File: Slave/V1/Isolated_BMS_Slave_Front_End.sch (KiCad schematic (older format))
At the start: 23 parts, among them J102 1935161, Q101 CPH6347-TL-W, U101 SI8641AB-B-IS1

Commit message: clear annotation
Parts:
- removed R103: RC0805JR-071KL, Resistors:R0805, symbol RC0805JR-071KL
- added R?: RC0805JR-07470KL, Resistors:R0805, symbol RC0805JR-07470KL
- renumbered C102 to C?, C101 to C?, C103 to C?, J102 to J?, Q101 to Q?, R101 to R?, U101 to U?
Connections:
- wire segments 115 -> 95
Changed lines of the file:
@@
 $EndDescr
 $Comp
-L CPH6347-TL-W Q101
+L CPH6347-TL-W Q?
 U 1 1 591B47DF
 P 2100 1300
-F 0 "Q101" V 2500 1300 60  0000 C CNN
+F 0 "Q?" V 2500 1300 60  0000 C CNN
 F 1 "CPH6347-TL-W" V 2400 1200 60  0000 C CNN
 F 2 "IC:TSOT-23-6" H 2200 400 60  0001 C CNN
@@
 $EndComp
 $Comp
-L 1935161 J102
+L 1935161 J?
 U 1 1 591B7F13
 P 900 1300
-F 0 "J102" H 800 1500 60  0000 C CNN
+F 0 "J?" H 800 1500 60  0000 C CNN
 F 1 "1935161" H 900 980 50  0001 C CNN
 F 2 "Connectors:1935161" H 900 390 30  0001 C CNN
@@
 CELL_Voltage
 $Comp
-L SI8641AB-B-IS1 U101
+L SI8641AB-B-IS1 U?
 U 1 1 591D60B1
 P 6200 4600
-F 0 "U101" H 6200 5400 60  0000 C CNN
+F 0 "U?" H 6200 5400 60  0000 C CNN
 F 1 "SI8641AB-B-IS1" H 6200 3750 60  0000 C CNN
 F 2 "IC:SOIC-16" H 6200 2800 60  0001 C CNN
@@
 $EndComp
 $Comp
-L AGND #PWR04
+L AGND #PWR?
 U 1 1 591D612D
 P 7600 4000
-F 0 "#PWR04" H 7600 3830 50  0001 C CNN
+F 0 "#PWR?" H 7600 3830 50  0001 C CNN
 F 1 "AGND" H 7600 3900 50  0000 C CNN
 F 2 "" H 7600 4100 60  0000 C CNN
@@
 $EndComp
 $Comp
-L 885012207098 C102
+L 885012207098 C?
 U 1 1 591D614C
 P 7100 3900
-F 0 "C102" H 7050 4060 60  0000 C CNN
+F 0 "C?" H 7050 4060 60  0000 C CNN
 F 1 "885012207098" H 7050 3550 60  0001 C CNN
 F 2 "Capacitors:C0805" H 7050 2950 60  0001 C CNN
@@
 $EndComp
 $Comp
-L 885012207098 C101
+L 885012207098 C?
 U 1 1 591D641D
 P 5400 3900
-F 0 "C101" H 5350 4060 60  0000 C CNN
+F 0 "C?" H 5350 4060 60  0000 C CNN
 F 1 "885012207098" H 5350 3550 60  0001 C CNN
 F 2 "Capacitors:C0805" H 5350 2950 60  0001 C CNN
@@
 SCLK_MCU
 $Comp
-L RC0805JR-074K7L R101
+L RC0805JR-074K7L R?
 U 1 1 591D91BB
 P 4700 5300
-F 0 "R101" H 4700 5380 60  0000 C CNN
+F 0 "R?" H 4700 5380 60  0000 C CNN
 F 1 "RC0805JR-074K7L" H 4700 5000 50  0001 C CNN
 F 2 "Resistors:R0805" H 4700 4400 30  0001 C CNN
@@
 $EndComp
 $Comp
-L 885012207098 C103
+L 885012207098 C?
 U 1 1 591D91D0
 P 5000 5500
-F 0 "C103" H 4950 5660 60  0000 C CNN
+F 0 "C?" H 4950 5660 60  0000 C CNN
 F 1 "885012207098" H 4950 5150 60  0001 C CNN
 F 2 "Capacitors:C0805" H 4950 4550 60  0001 C CNN
@@
 Text Label 1100 3500 0    60   ~ 0
 CELL_Voltage
-$Comp
-L RC0805JR-071KL R103
-U 1 1 592149D4
-P 2700 1500
-F 0 "R103" H 2700 1580 60  0000 C CNN
-F 1 "RC0805JR-071KL" H 2700 1200 50  0001 C CNN
-F 2 "Resistors:R0805" H 2700 600 30  0001 C CNN
-F 3 "http://www.yageo.com/documents/recent/PYu-RC_Group_51_RoHS_L_7.pdf" H 2700 550 30  0001 C CNN
-F 4 "Digikey" H 2700 1100 60  0001 C CNN "Supplier"
-F 5 "311-1.0KARCT-ND" H 2700 1000 60  0001 C CNN "Supplier Part Number"
-F 6 "Yageo" H 2700 900 60  0001 C CNN "Manufacturer"
-F 7 "RC0805JR-071KL" H 2700 800 60  0001 C CNN "Manufacturer Part Number"
-F 8 "RES SMD 1K OHM 5% 1/8W 0805" H 2700 700 60  0001 C CNN "Description"
-F 9 "1k" H 2700 1430 50  0000 C CNN "Resistance (Ohms)"
-F 10 "±5%" H 3110 1420 50  0001 C CNN "Tolerance (%)"
-F 11 "1/8W" H 2700 1360 50  0001 C CNN "Puissance (Watts)"
-	1    2700 1500
-	0    -1   -1   0
-$EndComp
-Wire Wire Line
-	1000 1200 1700 1200
-Wire Wire Line
-	1700 1200 1800 1200
+Wire Wire Line
+	1000 1200 1800 1200
 Wire Wire Line
 	1000 1300 1500 1300
 Wire Wire Line
-	1500 1300 1500 1700
-Wire Wire Line
-	1500 1700 1500 1800
+	1500 1300 1500 1800
 Wire Wire Line
 	1700 1100 1800 1100
@@
 Connection ~ 1700 1300
 Wire Wire Line
-	3600 1200 3700 1200
-Wire Wire Line
-	3700 1200 4700 1200
+	3600 1200 4700 1200
 Wire Wire Line
 	6700 5300 6800 5300
@@
 	5400 5300 5700 5300
 Wire Wire Line
-	6700 3900 6800 3900
-Wire Wire Line
-	6800 3900 6900 3900
+	6700 3900 6900 3900
 Wire Wire Line
 	6800 3900 6800 3600
 Connection ~ 6800 3900
 Wire Wire Line
-	7200 3900 7300 3900
-Wire Wire Line
-	7300 3900 7600 3900
+	7200 3900 7600 3900
 Wire Wire Line
 	6700 4100 7300 4100
@@
 	5600 3600 5600 3900
 Wire Wire Line
-	5500 3900 5600 3900
-Wire Wire Line
-	5600 3900 5700 3900
+	5500 3900 5700 3900
 Connection ~ 5600 3900
 Wire Wire Line
-	4500 3900 5000 3900
-Wire Wire Line
-	5000 3900 5200 3900
+	4500 3900 5200 3900
 Wire Wire Line
 	5700 4100 5000 4100
@@
 	6700 4300 7200 4300
 Wire Wire Line
-	6700 5100 7300 5100
-Wire Wire Line
-	7300 5100 7700 5100
-Wire Wire Line
-	7700 5100 7800 5100
+	6700 5100 7800 5100
 Wire Wire Line
 	7700 5100 7700 5200
@@
 Connection ~ 7700 5100
 Wire Wire Line
-	5000 5100 5000 5300
-Wire Wire Line
-	5000 5300 5000 5400
+	5000 5100 5000 5400
 Wire Wire Line
 	5000 5300 4900 5300
@@
 	3000 4700 3800 4700
 Wire Wire Line
-	3800 4700 3800 4900
-Wire Wire Line
-	3800 4900 3800 5000
+	3800 4700 3800 5000
 Wire Wire Line
 	3800 4900 4100 4900
@@
 	8700 2100 9600 2100
 $Comp
-L PWR_FLAG #FLG018
+L PWR_FLAG #FLG?
 U 1 1 5922363D
 P 1300 1700
-F 0 "#FLG018" H 1300 1600 60  0001 C CNN
+F 0 "#FLG?" H 1300 1600 60  0001 C CNN
 F 1 "PWR_FLAG" H 1300 1900 30  0000 C CNN
 F 2 "" H 1300 1700 60  0000 C CNN
@@
 Connection ~ 1500 1700
 Wire Wire Line
-	1700 1100 1700 1200
-Wire Wire Line
-	1700 1200 1700 1300
-Wire Wire Line
-	1700 1300 1700 1400
+	1700 1100 1700 1400
 $Comp
 L CPH6347-TL-W Q?
@@
 $EndComp
 Wire Wire Line
-	2400 1200 2700 1200
-Wire Wire Line
-	2700 1200 3000 1200
+	2400 1200 3000 1200
 Wire Wire Line
 	3600 1100 3700 1100
 Wire Wire Line
-	3700 1100 3700 1200
-Wire Wire Line
-	3700 1200 3700 1300
-Wire Wire Line
-	3700 1300 3700 1400
+	3700 1100 3700 1400
 Wire Wire Line
 	3700 1400 3600 1400
@@
 Connection ~ 2700 1200
 Wire Wire Line
-	2100 1800 2400 1800
-Wire Wire Line
-	2400 1800 2700 1800
-Wire Wire Line
-	2700 1800 2900 1800
-Wire Wire Line
-	2900 1800 3300 1800
+	2100 1800 3300 1800
 Wire Wire Line
 	3300 1800 3300 1500
@@
 	3000 2300 2900 2300
 Wire Wire Line
-	2900 2300 2900 2600
-Wire Wire Line
-	2900 2600 2900 2800
+	2900 2300 2900 2800
 Wire Wire Line
 	3000 2000 2900 2000
@@
 Text Label 9100 2700 0    60   ~ 0
 AGND
+$Comp
+L RC0805JR-07470KL R?
+U 1 1 59397104
+P 2700 1500
+F 0 "R?" H 2700 1580 60  0000 C CNN
+F 1 "RC0805JR-07470KL" H 2700 1200 50  0001 C CNN
+F 2 "Resistors:R0805" H 2700 600 30  0001 C CNN
+F 3 "http://www.yageo.com/documents/recent/PYu-RC_Group_51_RoHS_L_7.pdf" H 2700 550 30  0001 C CNN
+F 4 "Digikey" H 2700 1100 60  0001 C CNN "Supplier"
+F 5 "311-470KARCT-ND" H 2700 1000 60  0001 C CNN "Supplier Part Number"
+F 6 "Yageo" H 2700 900 60  0001 C CNN "Manufacturer"
+F 7 "RC0805JR-07470KL" H 2700 800 60  0001 C CNN "Manufacturer Part Number"
+F 8 "RES SMD 470K OHM 5% 1/8W 0805" H 2700 700 60  0001 C CNN "Description"
+F 9 "470k" H 2700 1430 50  0000 C CNN "Resistance (Ohms)"
+F 10 "±5%" H 3110 1420 50  0001 C CNN "Tolerance (%)"
+F 11 "1/8W" H 2700 1360 50  0001 C CNN "Puissance (Watts)"
+	1    2700 1500
+	0    -1   -1   0
+$EndComp
 $EndSCHEMATC

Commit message: add notes
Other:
- note added: "Mettre LED ROUGE \nqui allume si la cellule est inversé"
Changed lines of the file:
@@
 	0    -1   -1   0
 $EndComp
+Text Notes 600  2100 0    60   ~ 0
+Mettre LED ROUGE \nqui allume si la cellule est inversé
 $EndSCHEMATC

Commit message: add LED to reverse protection + balancing
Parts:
- added D?: 150080RS75000, Diodes:LED_0805_RED, symbol 150080RS75000
- added R?: RC0805JR-071KL, Resistors:R0805, symbol RC0805JR-071KL
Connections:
- wire segments 95 -> 98
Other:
- note removed: "Mettre LED ROUGE \nqui allume si la cellule est inversé"
- moved on the sheet: D?, Q?, R?, U?

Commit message: placing components
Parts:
- removed J?: 1935161, Connectors:1935161, symbol 1935161
- removed R? (x2): RC0805JR-07100RL, Resistors:R0805, symbol RC0805JR-07100RL
- removed R?: RC0805JR-074K7L, Resistors:R0805, symbol RC0805JR-074K7L
- added J501: 649002227222, Connectors:649002227222, symbol 649002227222
- added R510, R511: RC0805JR-074K7L, Resistors:R0805, symbol RC0805JR-074K7L
- added R514: RC0805JR-07470KL, Resistors:R0805, symbol RC0805JR-07470KL
- gave numbers to parts that had none: 21
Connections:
- net labels removed: MCU_GND
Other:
- note added: "Reverse polarity protection\n+\nSwitch"
- note removed: "Reverse polarity protection"

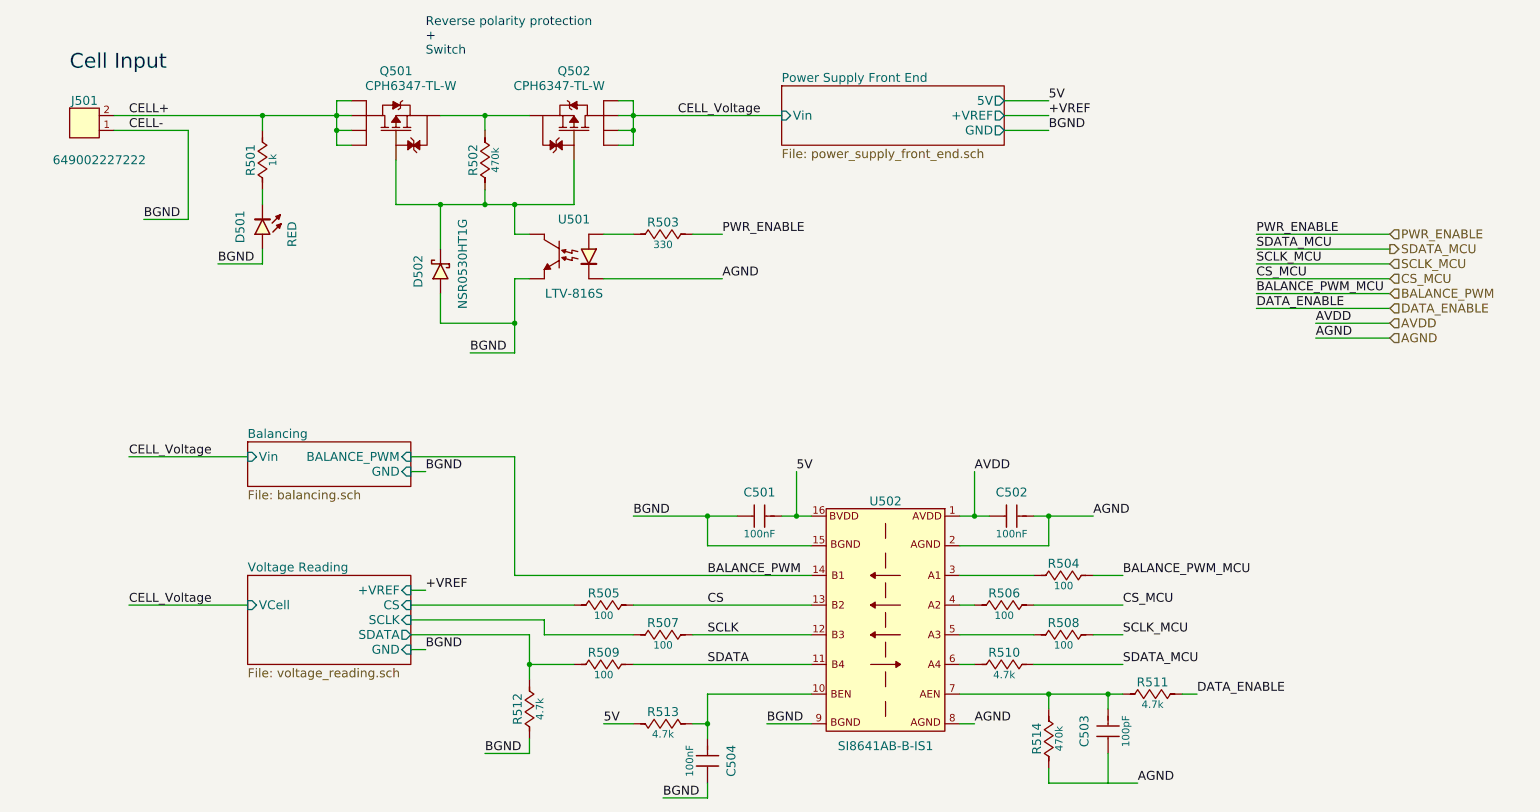
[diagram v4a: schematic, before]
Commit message: placing component on front end
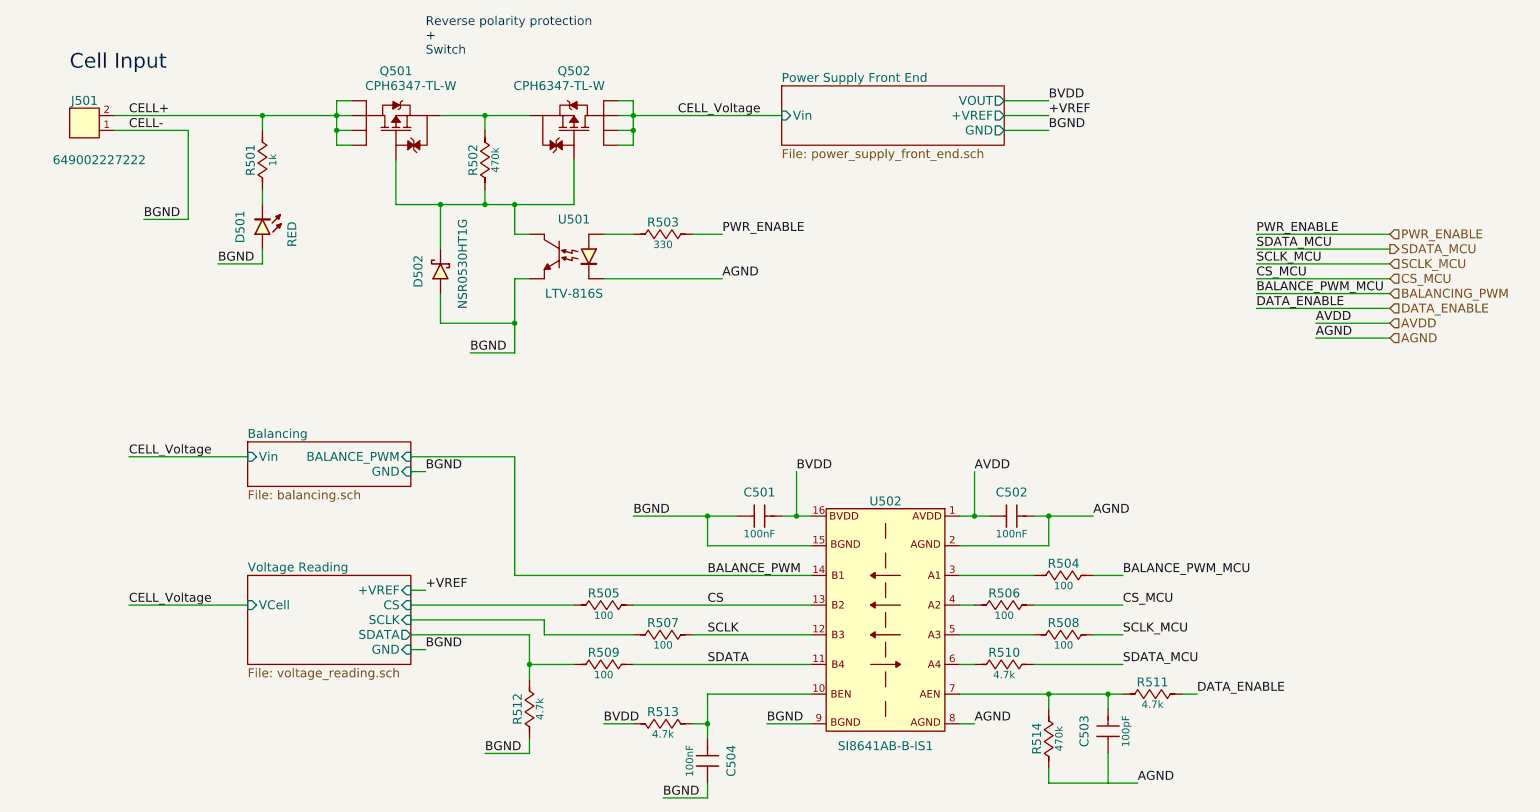
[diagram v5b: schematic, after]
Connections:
- net BALANCE_PWM: no longer R504.2
- net 5V renamed BVDD
- new net BALANCING_PWM: R504.2
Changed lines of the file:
@@
 F1 "power_supply_front_end.sch" 60
 F2 "Vin" I L 5500 1200 60
-F3 "5V" O R 7000 1100 60
-F4 "+VREF" O R 7000 1200 60
-F5 "GND" O R 7000 1300 60
+F3 "+VREF" O R 7000 1200 60
+F4 "GND" O R 7000 1300 60
+F5 "VOUT" O R 7000 1100 60
 $EndSheet
 Text Notes 3100 800  0    60   ~ 0
@@
 Connection ~ 7300 3900
 Wire Wire Line
-	5600 3600 5600 3900
-Wire Wire Line
 	5500 3900 5700 3900
 Connection ~ 5600 3900
@@
 CS_MCU
 Text HLabel 9600 2400 2    60   Input ~ 0
-BALANCE_PWM
+BALANCING_PWM
 Text HLabel 9600 2100 2    60   Output ~ 0
 SDATA_MCU
@@
 	7000 1100 7300 1100
 Text Label 7300 1100 0    60   ~ 0
-5V
+BVDD
 Text Label 7300 1200 0    60   ~ 0
 +VREF
@@
 	7000 1200 7300 1200
 Text Label 5600 3600 0    60   ~ 0
-5V
+BVDD
 Text Label 1200 1900 0    60   ~ 0
 BGND
@@
 AGND
 Text Label 4300 5300 0    60   ~ 0
-5V
+BVDD
 Text Label 3100 4400 0    60   ~ 0
 +VREF
@@
 	1    0    0    -1
 $EndComp
+Wire Wire Line
+	5600 3600 5600 3900
 $EndSCHEMATC

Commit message: adding 8 front end
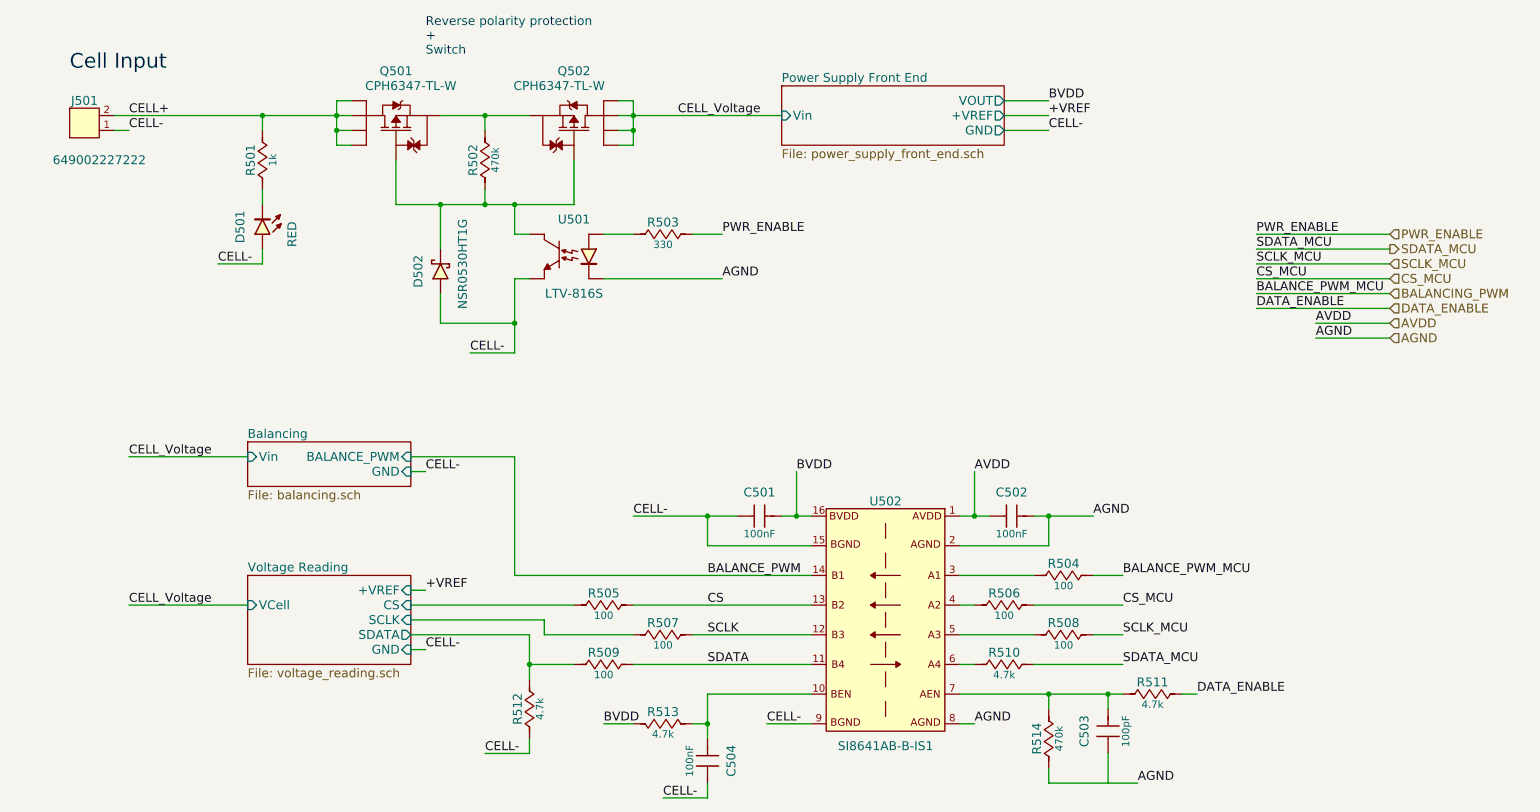
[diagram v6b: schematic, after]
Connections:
- net BGND renamed CELL-

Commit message: placed front end 1 to 5
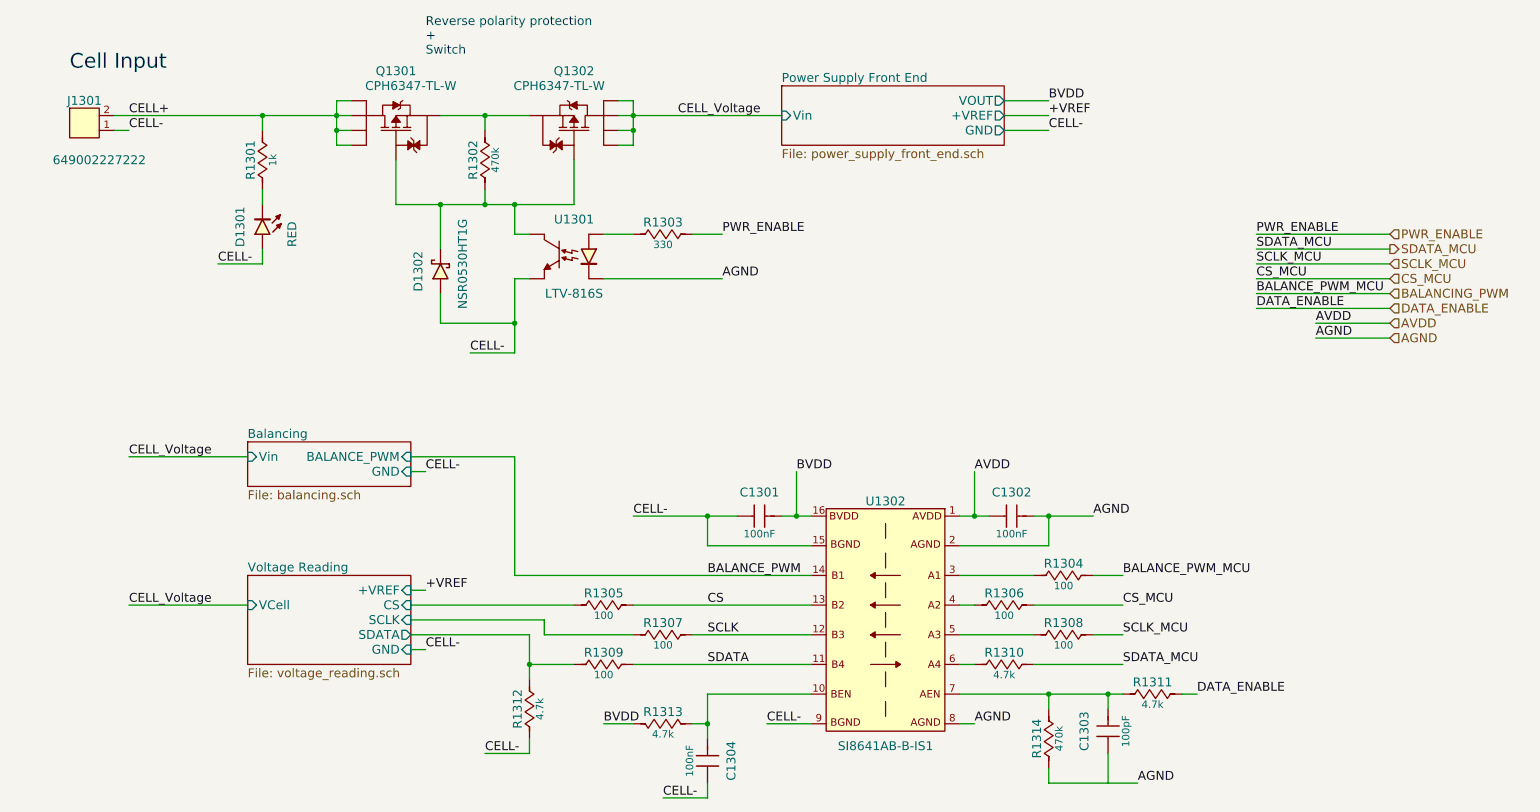
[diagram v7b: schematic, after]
